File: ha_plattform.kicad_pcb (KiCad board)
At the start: 2 copper layers, 55 x 55 mm, 12 parts, among them J3 Raspberry_Pi_2_3

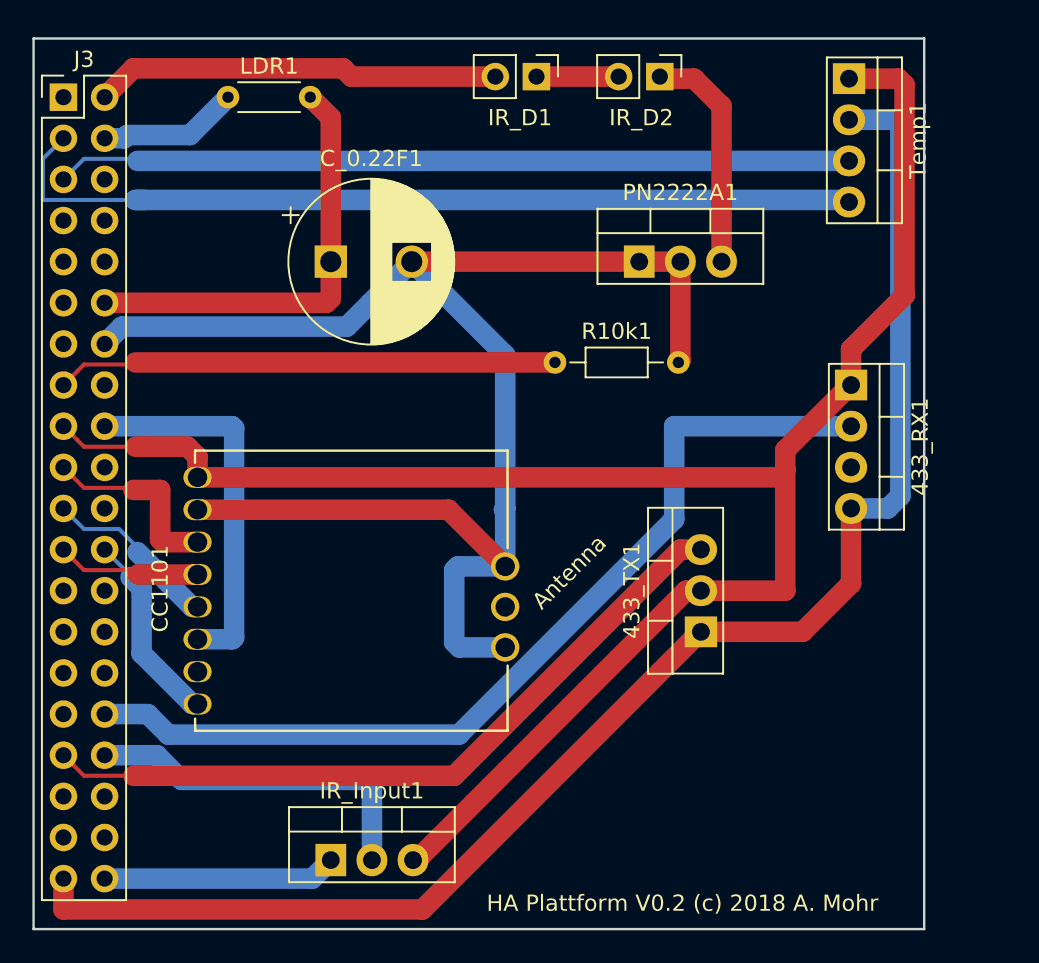
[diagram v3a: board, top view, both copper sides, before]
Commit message: Increased space between 433mhz modules
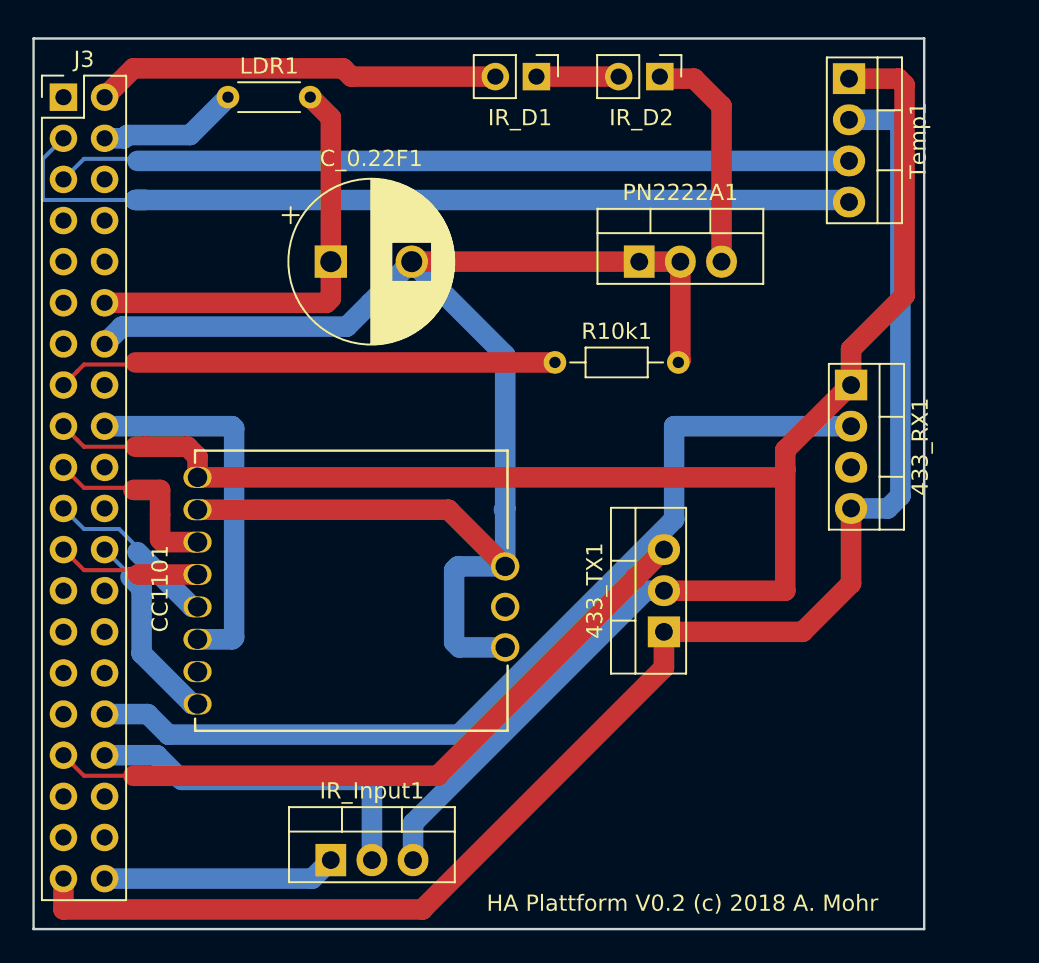
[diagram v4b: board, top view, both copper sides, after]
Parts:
- moved 433_TX1 2.29 mm to (58.9, 56.6)
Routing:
- net Net-(433_TX1-Pad3): track 45.7 -> 43.4 mm
- net Net-(433_RX1-Pad4): track 93.1 -> 94.4 mm
- net Net-(433_RX1-Pad1): track 114.3 -> 115.4 mm
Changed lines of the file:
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@@
     (thickness 1.6)
     (drawings 8)
-    (tracks 145)
+    (tracks 143)
     (zones 0)
     (modules 12)
@@
   )
   (module Package_TO_SOT_THT:TO-220-3_Vertical (layer F.Cu)
-    (at 61.214 56.642 90)
+    (at 58.928 56.642 90)
     (descr "TO-220-3, Vertical, RM 2.54mm, see https://www.vishay.com/docs/66542/to-220-1.pdf")
     (tags "TO-220-3 Vertical RM 2.54mm")
@@
     (effects (font (size 1 1) (thickness 0.1)))
   )
-  (gr_text Antenna (at 53.086 52.959 45) (layer F.SilkS)
+  (gr_text Antenna (at 53.086 52.959 45) (layer F.Fab)
     (effects (font (size 1 1) (thickness 0.1)))
   )
   (dimension 20.32 (width 0.3) (layer B.SilkS)
-    (gr_text "Size 433 TX" (at 55.407976 59.182 270) (layer B.SilkS)
+    (gr_text "Size 433 TX" (at 53.457179 59.168318 270) (layer B.SilkS)
       (effects (font (size 1.5 1.5) (thickness 0.3)))
     )
-    (feature1 (pts (xy 63.857976 69.342) (xy 56.921555 69.342)))
-    (feature2 (pts (xy 63.857976 49.022) (xy 56.921555 49.022)))
-    (crossbar (pts (xy 57.507976 49.022) (xy 57.507976 69.342)))
-    (arrow1a (pts (xy 57.507976 69.342) (xy 56.921555 68.215496)))
-    (arrow1b (pts (xy 57.507976 69.342) (xy 58.094397 68.215496)))
-    (arrow2a (pts (xy 57.507976 49.022) (xy 56.921555 50.148504)))
-    (arrow2b (pts (xy 57.507976 49.022) (xy 58.094397 50.148504)))
+    (feature1 (pts (xy 61.907179 69.328318) (xy 54.970758 69.328318)))
+    (feature2 (pts (xy 61.907179 49.008318) (xy 54.970758 49.008318)))
+    (crossbar (pts (xy 55.557179 49.008318) (xy 55.557179 69.328318)))
+    (arrow1a (pts (xy 55.557179 69.328318) (xy 54.970758 68.201814)))
+    (arrow1b (pts (xy 55.557179 69.328318) (xy 56.1436 68.201814)))
+    (arrow2a (pts (xy 55.557179 49.008318) (xy 54.970758 50.134822)))
+    (arrow2b (pts (xy 55.557179 49.008318) (xy 56.1436 50.134822)))
   )
   (dimension 30.48 (width 0.3) (layer B.SilkS)
@@
   (segment (start 37.211 71.882) (end 38.354 70.739) (width 1.27) (layer B.Cu) (net 16))
   (segment (start 24.384 71.882) (end 37.211 71.882) (width 1.27) (layer B.Cu) (net 16))
-  (segment (start 61.214 54.102) (end 61.1665 54.102) (width 0.25) (layer F.Cu) (net 17) (status 30))
   (segment (start 22.693999 44.791999) (end 21.844 43.942) (width 0.25) (layer F.Cu) (net 17) (status 30))
   (segment (start 22.693999 44.791999) (end 23.114 45.212) (width 0.25) (layer F.Cu) (net 17) (status 10))
@@
   (segment (start 30.124 45.832) (end 30.124 47.102) (width 1.27) (layer F.Cu) (net 17) (status 20))
   (segment (start 29.504 45.212) (end 30.124 45.832) (width 1.27) (layer F.Cu) (net 17))
-  (segment (start 61.214 54.102) (end 61.24942 54.102) (width 1.27) (layer F.Cu) (net 17) (status 30))
-  (segment (start 60.298498 54.102) (end 61.214 54.102) (width 1.27) (layer F.Cu) (net 17))
-  (segment (start 43.434 70.966498) (end 60.298498 54.102) (width 1.27) (layer F.Cu) (net 17))
   (segment (start 23.114 45.212) (end 26.035 45.212) (width 0.25) (layer F.Cu) (net 17))
   (segment (start 26.924 45.212) (end 26.289 45.212) (width 1.27) (layer F.Cu) (net 17))
   (segment (start 30.124 47.102) (end 66.294 47.102) (width 1.27) (layer F.Cu) (net 17))
-  (segment (start 61.2615 54.102) (end 61.214 54.102) (width 1.27) (layer F.Cu) (net 17) (status 30))
-  (segment (start 66.421 54.102) (end 61.214 54.102) (width 1.27) (layer F.Cu) (net 17))
-  (segment (start 66.421 46.625) (end 66.421 54.102) (width 1.27) (layer F.Cu) (net 17))
-  (segment (start 70.4375 41.402) (end 70.485 41.402) (width 1.27) (layer F.Cu) (net 17))
-  (segment (start 66.421009 45.418491) (end 70.4375 41.402) (width 1.27) (layer F.Cu) (net 17))
-  (segment (start 66.421009 46.624991) (end 66.421009 45.418491) (width 1.27) (layer F.Cu) (net 17))
-  (segment (start 66.421 46.625) (end 66.421009 46.624991) (width 1.27) (layer F.Cu) (net 17))
   (segment (start 73.406 22.479) (end 70.358 22.479) (width 1.27) (layer F.Cu) (net 17))
   (segment (start 73.787 35.8775) (end 73.787 22.86) (width 1.27) (layer F.Cu) (net 17))
@@
   (segment (start 70.485 41.402) (end 70.485 39.1795) (width 1.27) (layer F.Cu) (net 17))
   (segment (start 70.485 39.1795) (end 73.787 35.8775) (width 1.27) (layer F.Cu) (net 17))
+  (segment (start 66.421009 46.624991) (end 66.421009 45.418491) (width 1.27) (layer F.Cu) (net 17))
+  (segment (start 70.4375 41.402) (end 70.485 41.402) (width 1.27) (layer F.Cu) (net 17))
+  (segment (start 58.928 54.102) (end 66.421 54.102) (width 1.27) (layer F.Cu) (net 17))
+  (segment (start 66.421009 45.418491) (end 70.4375 41.402) (width 1.27) (layer F.Cu) (net 17))
+  (segment (start 66.421 46.625) (end 66.421009 46.624991) (width 1.27) (layer F.Cu) (net 17))
+  (segment (start 66.421 54.102) (end 66.421 46.625) (width 1.27) (layer F.Cu) (net 17))
+  (segment (start 43.434 68.469) (end 43.434 70.739) (width 1.27) (layer B.Cu) (net 17))
+  (segment (start 57.801 54.102) (end 43.434 68.469) (width 1.27) (layer B.Cu) (net 17))
+  (segment (start 58.928 54.102) (end 57.801 54.102) (width 1.27) (layer B.Cu) (net 17))
   (segment (start 46.264802 62.992) (end 59.560002 49.6968) (width 1.27) (layer B.Cu) (net 18))
   (segment (start 28.321 62.992) (end 46.264802 62.992) (width 1.27) (layer B.Cu) (net 18))
@@
   (segment (start 27.051 61.722) (end 28.321 62.992) (width 1.27) (layer B.Cu) (net 18))
   (segment (start 59.560002 43.942) (end 70.485 43.942) (width 1.27) (layer B.Cu) (net 18))
-  (segment (start 61.214 56.642) (end 67.4965 56.642) (width 1.27) (layer F.Cu) (net 19) (status 10))
-  (segment (start 61.214 56.642) (end 61.1665 56.642) (width 0.25) (layer B.Cu) (net 19) (status 30))
-  (segment (start 61.1665 56.642) (end 61.214 56.642) (width 1.27) (layer F.Cu) (net 19))
   (segment (start 21.844 73.787) (end 44.0215 73.787) (width 1.27) (layer F.Cu) (net 19))
-  (segment (start 44.0215 73.787) (end 61.1665 56.642) (width 1.27) (layer F.Cu) (net 19))
   (segment (start 21.844 71.882) (end 21.844 73.787) (width 1.27) (layer F.Cu) (net 19))
-  (segment (start 70.485 53.6535) (end 70.485 49.022) (width 1.27) (layer F.Cu) (net 19))
-  (segment (start 67.4965 56.642) (end 70.485 53.6535) (width 1.27) (layer F.Cu) (net 19))
   (segment (start 72.755 49.022) (end 73.533 48.244) (width 1.27) (layer B.Cu) (net 19))
   (segment (start 70.485 49.022) (end 72.755 49.022) (width 1.27) (layer B.Cu) (net 19))
@@
   (segment (start 73.152 25.019) (end 70.358 25.019) (width 1.27) (layer B.Cu) (net 19))
   (segment (start 73.533 25.4) (end 73.152 25.019) (width 1.27) (layer B.Cu) (net 19))
-  (segment (start 61.214 51.562) (end 59.944 51.562) (width 1.27) (layer F.Cu) (net 20) (status 10))
-  (segment (start 59.944 51.562) (end 45.974 65.532) (width 1.27) (layer F.Cu) (net 20))
-  (segment (start 45.974 65.532) (end 26.924 65.532) (width 1.27) (layer F.Cu) (net 20))
+  (segment (start 70.485 53.6535) (end 70.485 49.022) (width 1.27) (layer F.Cu) (net 19))
+  (segment (start 58.928 56.642) (end 67.4965 56.642) (width 1.27) (layer F.Cu) (net 19))
+  (segment (start 67.4965 56.642) (end 70.485 53.6535) (width 1.27) (layer F.Cu) (net 19))
+  (segment (start 44.0215 73.771) (end 44.0215 73.787) (width 1.27) (layer F.Cu) (net 19))
+  (segment (start 58.928 58.8645) (end 44.0215 73.771) (width 1.27) (layer F.Cu) (net 19))
+  (segment (start 58.928 56.642) (end 58.928 58.8645) (width 1.27) (layer F.Cu) (net 19))
   (segment (start 23.114 65.532) (end 21.844 64.262) (width 0.25) (layer F.Cu) (net 20) (status 20))
   (segment (start 26.924 65.532) (end 26.162 65.532) (width 1.27) (layer F.Cu) (net 20))
   (segment (start 26.162 65.532) (end 23.114 65.532) (width 0.25) (layer F.Cu) (net 20))
+  (segment (start 57.16599 53.32401) (end 44.958 65.532) (width 1.27) (layer F.Cu) (net 20))
+  (segment (start 58.928 51.562) (end 57.16599 53.32401) (width 1.27) (layer F.Cu) (net 20))
+  (segment (start 44.958 65.532) (end 26.924 65.532) (width 1.27) (layer F.Cu) (net 20))
 )

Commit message: fixed layout issues. moved led to front. rerouted whole board
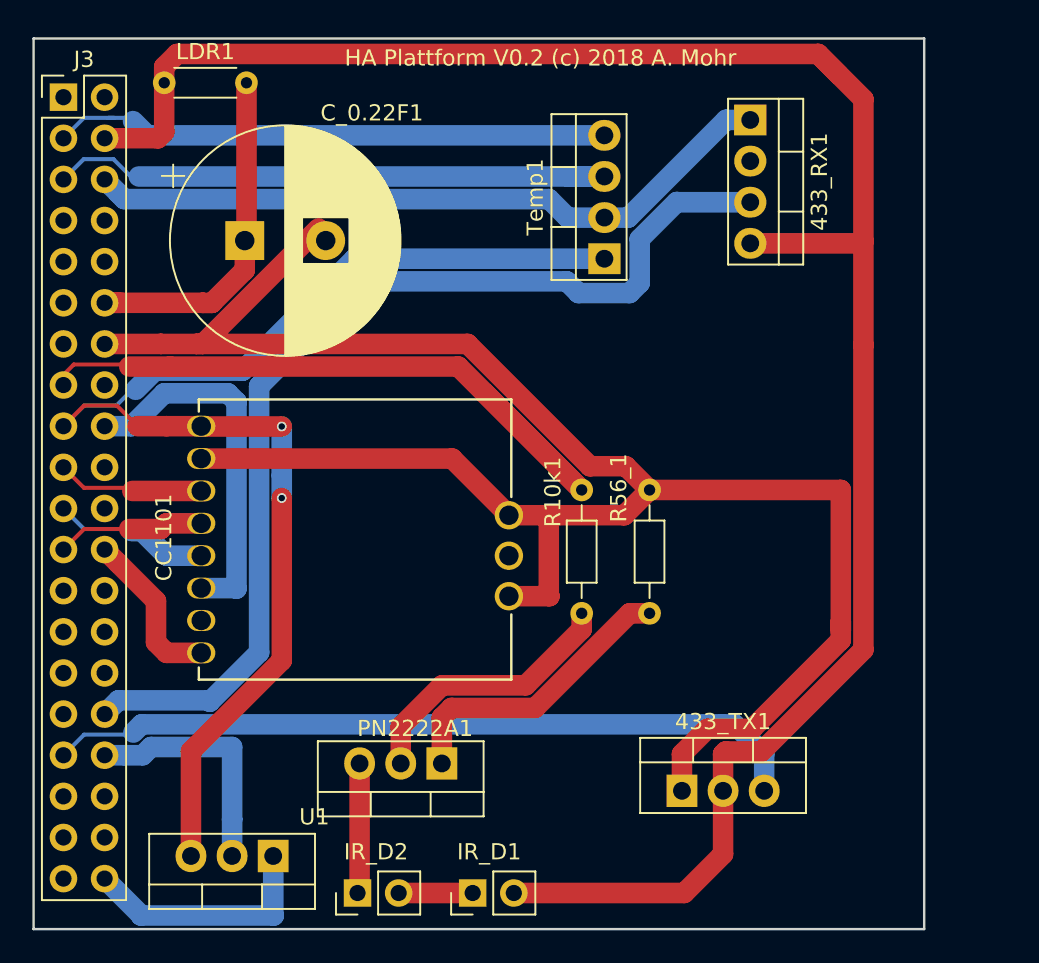
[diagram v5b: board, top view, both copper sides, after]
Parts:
- removed IR_Input1: TSOP382xx, Package_TO_SOT_THT:TO-220-3_Vertical
- added R56_1: R, Resistor_THT:R_Axial_DIN0204_L3.6mm_D1.6mm_P7.62mm_Horizontal, F.Cu at (58.0, 55.5)
- added U1: TSOP45xx_0, Package_TO_SOT_THT:TO-220-3_Vertical, F.Cu at (34.8, 70.5)
- C_0.22F1: footprint Capacitor_THT:CP_Radial_D10.0mm_P5.00mm -> Capacitor_THT:CP_Radial_D14.0mm_P5.00mm
- moved IR_D2 53.8 mm to (40.0, 72.8), turned to 90 degrees
- moved IR_D1 50.6 mm to (47.1, 72.8), turned to 90 degrees
- moved PN2222A1 33.3 mm to (45.2, 64.8), turned to 180 degrees
- moved Temp1 18.8 mm to (55.2, 33.6), turned to 90 degrees
- moved 433_RX1 17.5 mm to (64.3, 25.0)
- moved 433_TX1 9.88 mm to (60.0, 66.5), turned to 0 degrees
- moved R10k1 8.05 mm to (53.8, 47.9), turned to 270 degrees
- moved C_0.22F1 5.47 mm to (33.0, 32.5)
- moved LDR1 4.04 mm to (28.1, 22.7)
- moved CC1101 3.17 mm to (39.9, 50.9)
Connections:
- 433_RX1 pad 3: (no net) -> Net-(433_RX1-Pad3)
- 433_TX1 pad 1: Net-(433_RX1-Pad4) -> Net-(433_TX1-Pad1)
- 433_TX1 pad 2: Net-(433_RX1-Pad1) -> Net-(433_RX1-Pad4)
- CC1101 pad 1: Net-(433_RX1-Pad1) -> Net-(CC1101-Pad1)
- CC1101 pad 10: (no net) -> Net-(CC1101-Pad10)
- CC1101 pad 11: Net-(CC1101-Pad11) -> Net-(433_TX1-Pad1)
- CC1101 pad 2: Net-(CC1101-Pad11) -> Net-(433_TX1-Pad1)
- CC1101 pad 7: (no net) -> Net-(CC1101-Pad7)
- CC1101 pad 9: Net-(CC1101-Pad11) -> Net-(433_TX1-Pad1)
- C_0.22F1 pad 2: Net-(CC1101-Pad11) -> Net-(433_TX1-Pad1)
- IR_D1 pad 2: Net-(IR_D1-Pad2) -> Net-(433_RX1-Pad4)
- J3 pad 1: (no net) -> Net-(J3-Pad1)
- J3 pad 10: (no net) -> Net-(J3-Pad10)
- J3 pad 11: (no net) -> Net-(J3-Pad11)
- J3 pad 13: (no net) -> Net-(J3-Pad13)
- J3 pad 14: Net-(CC1101-Pad11) -> Net-(433_TX1-Pad1)
- J3 pad 16: (no net) -> Net-(J3-Pad16)
- J3 pad 17: Net-(433_RX1-Pad1) -> Net-(CC1101-Pad1)
- J3 pad 2: Net-(IR_D1-Pad2) -> Net-(J3-Pad2)
- J3 pad 20: (no net) -> Net-(J3-Pad20)
- J3 pad 22: (no net) -> Net-(J3-Pad22)
- J3 pad 25: (no net) -> Net-(J3-Pad25)
- J3 pad 26: (no net) -> Net-(J3-Pad26)
- J3 pad 27: (no net) -> Net-(J3-Pad27)
- J3 pad 28: (no net) -> Net-(J3-Pad28)
- J3 pad 29: (no net) -> Net-(J3-Pad29)
- J3 pad 30: (no net) -> Net-(J3-Pad30)
- J3 pad 31: (no net) -> Net-(J3-Pad31)
- J3 pad 32: Net-(433_RX1-Pad2) -> Net-(433_RX1-Pad3)
- J3 pad 35: (no net) -> Net-(J3-Pad35)
- J3 pad 36: (no net) -> Net-(J3-Pad36)
- J3 pad 37: (no net) -> Net-(J3-Pad37)
- J3 pad 38: (no net) -> Net-(J3-Pad38)
- J3 pad 39: Net-(433_RX1-Pad4) -> Net-(J3-Pad39)
- J3 pad 4: Net-(J3-Pad4) -> Net-(433_RX1-Pad4)
- J3 pad 6: (no net) -> Net-(433_RX1-Pad1)
- J3 pad 7: (no net) -> Net-(J3-Pad7)
- J3 pad 8: (no net) -> Net-(J3-Pad8)
- J3 pad 9: (no net) -> Net-(J3-Pad9)
- LDR1 pad 1: Net-(J3-Pad4) -> Net-(433_RX1-Pad4)
- PN2222A1 pad 1: Net-(CC1101-Pad11) -> Net-(PN2222A1-Pad1)
- PN2222A1 pad 2: Net-(CC1101-Pad11) -> Net-(PN2222A1-Pad2)
- R10k1 pad 2: Net-(CC1101-Pad11) -> Net-(PN2222A1-Pad2)
- Temp1 pad 1: Net-(433_RX1-Pad1) -> Net-(CC1101-Pad1)
- Temp1 pad 2: Net-(433_RX1-Pad4) -> Net-(433_RX1-Pad1)
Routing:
- net Net-(433_TX1-Pad1): track 0.00 -> 121.8 mm
- net Net-(CC1101-Pad11): track 97.2 -> 0.00 mm
- net Net-(CC1101-Pad1): track 0.00 -> 81.1 mm, vias 0 -> 2
- net Net-(433_RX1-Pad1): track 115.4 -> 43.4 mm
- net Net-(433_RX1-Pad3): track 0.00 -> 64.9 mm
- net Net-(433_RX1-Pad2): track 57.9 -> 0.00 mm
- net Net-(433_RX1-Pad4): track 94.4 -> 127.0 mm
- net Net-(IR_D1-Pad2): track 25.1 -> 0.00 mm
- net Net-(J3-Pad3): track 54.8 -> 34.9 mm
- net Net-(PN2222A1-Pad1): track 0.00 -> 18.3 mm
- net Net-(PN2222A1-Pad2): track 0.00 -> 16.9 mm
- net Net-(J3-Pad15): track 30.5 -> 44.6 mm
- net Net-(J3-Pad5): track 48.9 -> 36.6 mm
- net Net-(J3-Pad4): track 9.31 -> 0.00 mm
- net Net-(J3-Pad34): track 22.1 -> 14.8 mm
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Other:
- board text removed: "Antenna"

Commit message: Updated images and gerber files. Added don't trash and open hardware symbol
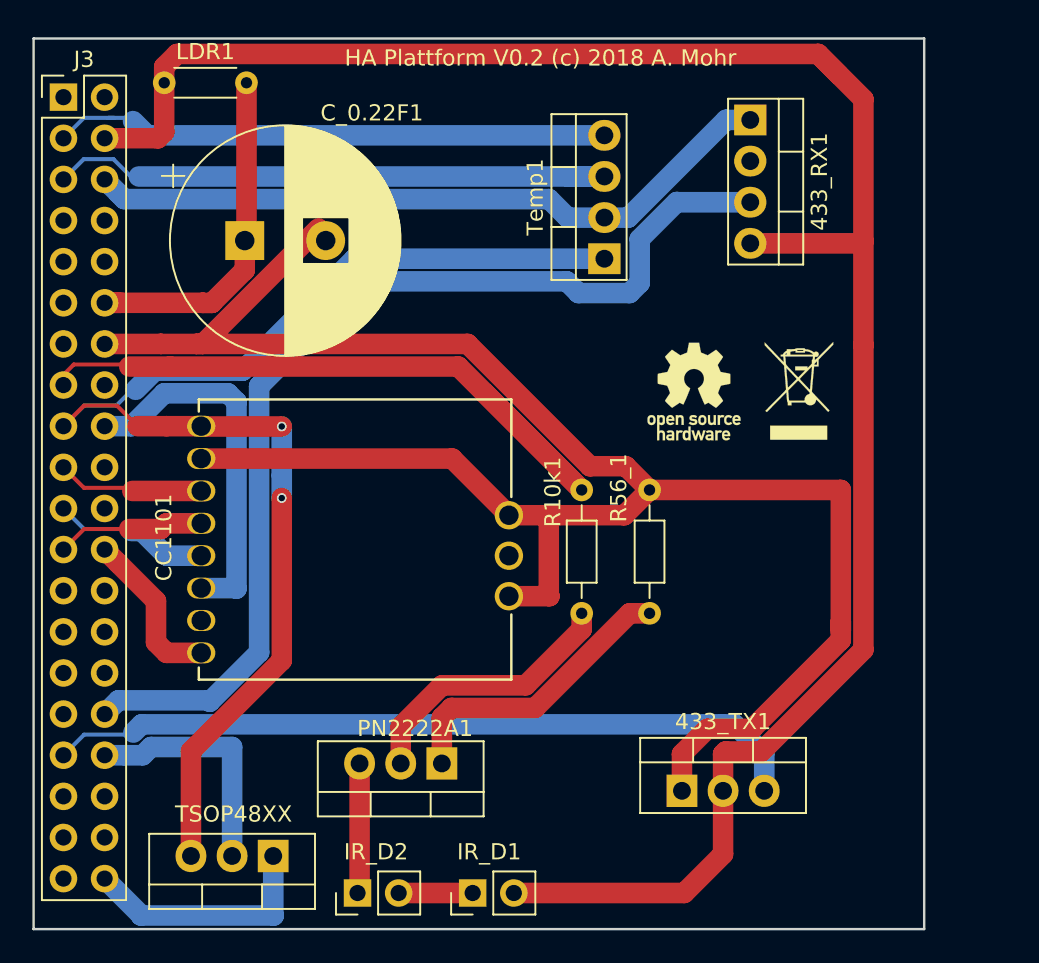
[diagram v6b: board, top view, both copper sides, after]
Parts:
- added REF**: OSHW-Logo_5.7x6mm_SilkScreen, Symbol:OSHW-Logo_5.7x6mm_SilkScreen, F.Cu at (60.8, 41.8)
- added REF**: WEEE-Logo_4.2x6mm_SilkScreen, Symbol:WEEE-Logo_4.2x6mm_SilkScreen, F.Cu at (67.3, 41.8)
- renumbered U1 to TSOP48XX
